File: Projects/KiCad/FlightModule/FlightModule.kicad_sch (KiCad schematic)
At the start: 53 parts, among them J1 Conn_01x05_Socket, J2 Conn_01x04_Pin, J3 Conn_01x05_Pin, J4 Conn_01x02_Pin, J5 Conn_01x02_Pin, J6 Conn_01x02_Pin, J7 Conn_01x02_Pin, J8 Conn_01x02_Pin, SW1 SW_Push, SW2 SW_Push, U1 NUCLEO-F303K8, U2 MCP2562-E-P, U3 TLP222A, U4 TLP222A, U5 MB85RS2MT

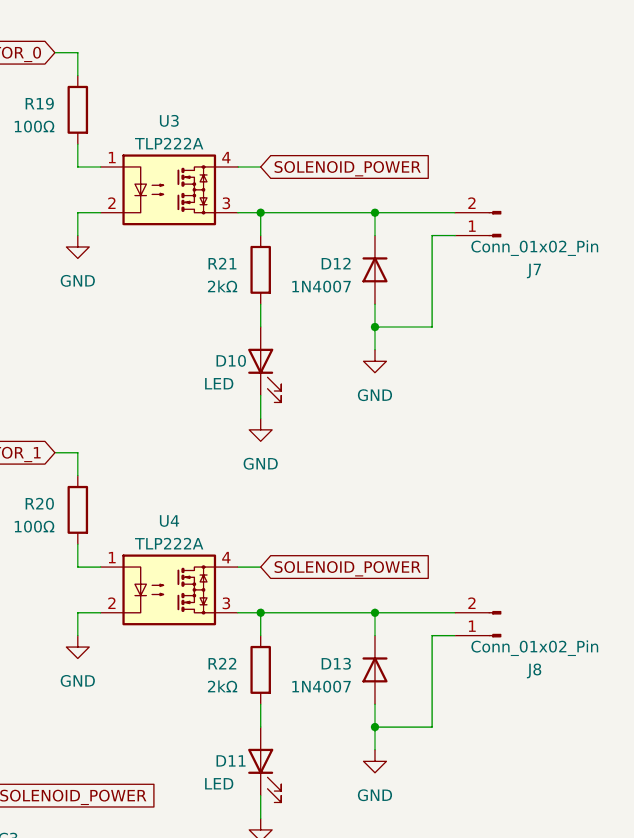
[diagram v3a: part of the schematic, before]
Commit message: ソレノイドのサージキラー回路に整流用ダイオードを追加
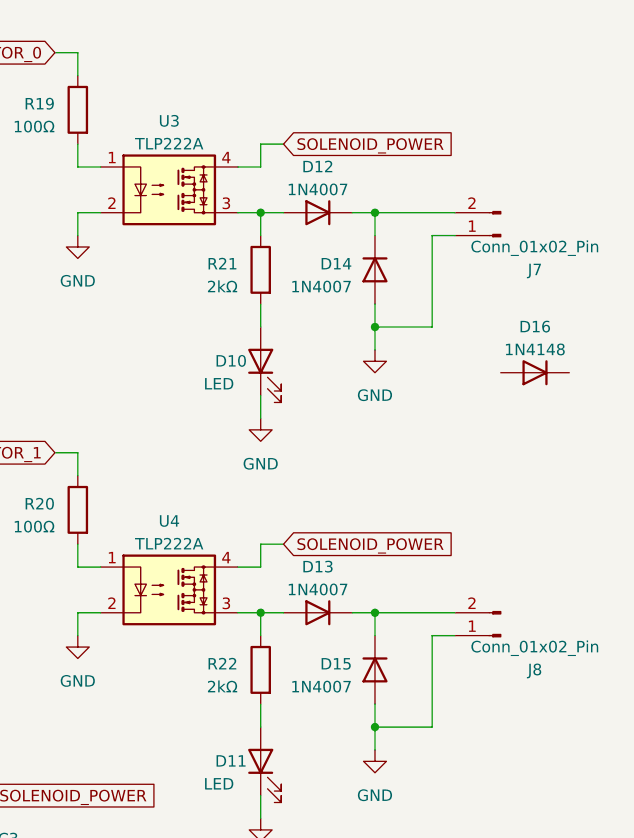
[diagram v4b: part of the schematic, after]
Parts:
- added D12, D13: 1N4007, Diode_THT:D_DO-41_SOD81_P10.16mm_Horizontal, symbol Diode:1N4007
- added D16: 1N4148, Diode_THT:D_DO-35_SOD27_P7.62mm_Horizontal, symbol Diode:1N4148
- renumbered D12 to D14, D13 to D15
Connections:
- net at R22.1, U4.3: now also D13.2 (A); no longer D15.1 (K), J8.2 (Pin_2)
- net at D14.1 (K), J7.2 (Pin_2): now also D12.1 (K); no longer R21.1, U3.3
- new net: D12.2 (A), R21.1, U3.3
- new net: D13.1 (K), D15.1 (K), J8.2 (Pin_2)
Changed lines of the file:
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@@
 (kicad_sch (version 20230121) (generator eeschema)
   (paper "A4")
+  (junction (at 246.38 38.1) (diameter 0) (color 0 0 0 0)
+  )
   (junction (at 115.57 110.49) (diameter 0) (color 0 0 0 0)
   )
@@
   (junction (at 163.83 114.3) (diameter 0) (color 0 0 0 0)
   )
+  (junction (at 222.25 143.51) (diameter 0) (color 0 0 0 0)
+  )
+  (junction (at 190.5 114.3) (diameter 0) (color 0 0 0 0)
+  )
+  (junction (at 213.36 102.87) (diameter 0) (color 0 0 0 0)
+  )
+  (junction (at 259.08 38.1) (diameter 0) (color 0 0 0 0)
+  )
+  (junction (at 229.87 140.97) (diameter 0) (color 0 0 0 0)
+  )
   (junction (at 246.38 82.55) (diameter 0) (color 0 0 0 0)
   )
-  (junction (at 222.25 143.51) (diameter 0) (color 0 0 0 0)
-  )
   (junction (at 259.08 82.55) (diameter 0) (color 0 0 0 0)
-  )
-  (junction (at 190.5 114.3) (diameter 0) (color 0 0 0 0)
-  )
-  (junction (at 246.38 38.1) (diameter 0) (color 0 0 0 0)
-  )
-  (junction (at 213.36 102.87) (diameter 0) (color 0 0 0 0)
-  )
-  (junction (at 259.08 38.1) (diameter 0) (color 0 0 0 0)
-  )
-  (junction (at 229.87 140.97) (diameter 0) (color 0 0 0 0)
   )
   (junction (at 242.57 151.13) (diameter 0) (color 0 0 0 0)
@@
     (stroke (width 0) (type default))
   )
-  (wire (pts (xy 243.84 77.47) (xy 246.38 77.47))
+  (wire (pts (xy 246.38 74.93) (xy 248.92 74.93))
     (stroke (width 0) (type default))
   )
@@
     (stroke (width 0) (type default))
   )
+  (wire (pts (xy 246.38 74.93) (xy 246.38 77.47))
+    (stroke (width 0) (type default))
+  )
   (wire (pts (xy 43.18 31.75) (xy 48.26 31.75))
     (stroke (width 0) (type default))
@@
     (stroke (width 0) (type default))
   )
+  (wire (pts (xy 246.38 30.48) (xy 246.38 33.02))
+    (stroke (width 0) (type default))
+  )
   (wire (pts (xy 27.94 34.29) (xy 40.64 34.29))
     (stroke (width 0) (type default))
@@
     (stroke (width 0) (type default))
   )
-  (wire (pts (xy 246.38 82.55) (xy 259.08 82.55))
-    (stroke (width 0) (type default))
-  )
   (wire (pts (xy 43.18 34.29) (xy 48.26 34.29))
     (stroke (width 0) (type default))
@@
     (stroke (width 0) (type default))
   )
-  (wire (pts (xy 246.38 38.1) (xy 259.08 38.1))
-    (stroke (width 0) (type default))
-  )
   (bus (pts (xy 43.18 53.34) (xy 43.18 55.88))
     (stroke (width 0) (type default))
@@
     (stroke (width 0) (type default))
   )
+  (wire (pts (xy 256.54 38.1) (xy 259.08 38.1))
+    (stroke (width 0) (type default))
+  )
   (wire (pts (xy 259.08 38.1) (xy 259.08 40.64))
     (stroke (width 0) (type default))
@@
     (stroke (width 0) (type default))
   )
+  (wire (pts (xy 246.38 82.55) (xy 248.92 82.55))
+    (stroke (width 0) (type default))
+  )
   (wire (pts (xy 190.5 124.46) (xy 190.5 127))
     (stroke (width 0) (type default))
@@
     (stroke (width 0) (type default))
   )
+  (wire (pts (xy 246.38 38.1) (xy 248.92 38.1))
+    (stroke (width 0) (type default))
+  )
   (wire (pts (xy 139.7 43.18) (xy 139.7 45.72))
     (stroke (width 0) (type default))
@@
     (stroke (width 0) (type default))
   )
+  (wire (pts (xy 246.38 77.47) (xy 243.84 77.47))
+    (stroke (width 0) (type default))
+  )
   (wire (pts (xy 259.08 82.55) (xy 259.08 85.09))
     (stroke (width 0) (type default))
@@
     (stroke (width 0) (type default))
   )
+  (wire (pts (xy 246.38 33.02) (xy 243.84 33.02))
+    (stroke (width 0) (type default))
+  )
   (wire (pts (xy 242.57 130.81) (xy 242.57 133.35))
     (stroke (width 0) (type default))
@@
     (stroke (width 0) (type default))
   )
+  (wire (pts (xy 256.54 82.55) (xy 259.08 82.55))
+    (stroke (width 0) (type default))
+  )
   (wire (pts (xy 134.62 110.49) (xy 137.16 110.49))
     (stroke (width 0) (type default))
@@
     (stroke (width 0) (type default))
   )
-  (wire (pts (xy 243.84 33.02) (xy 246.38 33.02))
+  (wire (pts (xy 246.38 30.48) (xy 248.92 30.48))
     (stroke (width 0) (type default))
   )
@@
     )
   )
-  (global_label "SOLENOID_POWER" (shape input) (at 246.38 33.02 0) (fields_autoplaced)
-    (effects (font (size 1.27 1.27)) (justify left))
-    (property "Intersheetrefs" "${INTERSHEET_REFS}" (at 265.9772 33.02 0)
+  (global_label "SOLENOID_POWER" (shape input) (at 248.92 30.48 0) (fields_autoplaced)
+    (effects (font (size 1.27 1.27)) (justify left))
+    (property "Intersheetrefs" "${INTERSHEET_REFS}" (at 268.5172 30.48 0)
       (effects (font (size 1.27 1.27)) (justify left) hide)
     )
@@
     )
   )
-  (global_label "SOLENOID_POWER" (shape input) (at 246.38 77.47 0) (fields_autoplaced)
-    (effects (font (size 1.27 1.27)) (justify left))
-    (property "Intersheetrefs" "${INTERSHEET_REFS}" (at 265.9772 77.47 0)
+  (global_label "SOLENOID_POWER" (shape input) (at 248.92 74.93 0) (fields_autoplaced)
+    (effects (font (size 1.27 1.27)) (justify left))
+    (property "Intersheetrefs" "${INTERSHEET_REFS}" (at 268.5172 74.93 0)
       (effects (font (size 1.27 1.27)) (justify left) hide)
     )
@@
   (symbol (lib_id "Diode:1N4007") (at 259.08 44.45 90) (mirror x) (unit 1)
     (in_bom yes) (on_board yes) (dnp no) (fields_autoplaced)
-    (property "Reference" "D12" (at 256.54 43.815 90)
+    (property "Reference" "D14" (at 256.54 43.815 90)
       (effects (font (size 1.27 1.27)) (justify left))
     )
@@
       (project "FlightModule"
         (path "/ea1ed597-7cd3-4340-902e-bdce8f2d7a62"
-          (reference "D12") (unit 1)
+          (reference "D14") (unit 1)
         )
       )
@@
         (path "/ea1ed597-7cd3-4340-902e-bdce8f2d7a62"
           (reference "#PWR017") (unit 1)
+        )
+      )
+    )
+  )
+  (symbol (lib_id "Diode:1N4148") (at 276.86 55.88 180) (unit 1)
+    (in_bom yes) (on_board yes) (dnp no) (fields_autoplaced)
+    (property "Reference" "D16" (at 276.86 50.8 0)
+      (effects (font (size 1.27 1.27)))
+    )
+    (property "Value" "1N4148" (at 276.86 53.34 0)
+      (effects (font (size 1.27 1.27)))
+    )
+    (property "Footprint" "Diode_THT:D_DO-35_SOD27_P7.62mm_Horizontal" (at 276.86 55.88 0)
+      (effects (font (size 1.27 1.27)) hide)
+    )
+    (property "Datasheet" "https://assets.nexperia.com/documents/data-sheet/1N4148_1N4448.pdf" (at 276.86 55.88 0)
+      (effects (font (size 1.27 1.27)) hide)
+    )
+    (property "Sim.Device" "D" (at 276.86 55.88 0)
+      (effects (font (size 1.27 1.27)) hide)
+    )
+    (property "Sim.Pins" "1=K 2=A" (at 276.86 55.88 0)
+      (effects (font (size 1.27 1.27)) hide)
+    )
+    (pin "1")
+    (pin "2")
+    (instances
+      (project "FlightModule"
+        (path "/ea1ed597-7cd3-4340-902e-bdce8f2d7a62"
+          (reference "D16") (unit 1)
         )
       )
@@
         (path "/ea1ed597-7cd3-4340-902e-bdce8f2d7a62"
           (reference "R12") (unit 1)
+        )
+      )
+    )
+  )
+  (symbol (lib_id "Diode:1N4007") (at 252.73 82.55 0) (mirror y) (unit 1)
+    (in_bom yes) (on_board yes) (dnp no) (fields_autoplaced)
+    (property "Reference" "D13" (at 252.73 77.47 0)
+      (effects (font (size 1.27 1.27)))
+    )
+    (property "Value" "1N4007" (at 252.73 80.01 0)
+      (effects (font (size 1.27 1.27)))
+    )
+    (property "Footprint" "Diode_THT:D_DO-41_SOD81_P10.16mm_Horizontal" (at 252.73 86.995 0)
+      (effects (font (size 1.27 1.27)) hide)
+    )
+    (property "Datasheet" "http://www.vishay.com/docs/88503/1n4001.pdf" (at 252.73 82.55 0)
+      (effects (font (size 1.27 1.27)) hide)
+    )
+    (property "Sim.Device" "D" (at 252.73 82.55 0)
+      (effects (font (size 1.27 1.27)) hide)
+    )
+    (property "Sim.Pins" "1=K 2=A" (at 252.73 82.55 0)
+      (effects (font (size 1.27 1.27)) hide)
+    )
+    (pin "1")
+    (pin "2")
+    (instances
+      (project "FlightModule"
+        (path "/ea1ed597-7cd3-4340-902e-bdce8f2d7a62"
+          (reference "D13") (unit 1)
         )
       )
@@
     )
   )
+  (symbol (lib_id "Diode:1N4007") (at 252.73 38.1 0) (mirror y) (unit 1)
+    (in_bom yes) (on_board yes) (dnp no) (fields_autoplaced)
+    (property "Reference" "D12" (at 252.73 33.02 0)
+      (effects (font (size 1.27 1.27)))
+    )
+    (property "Value" "1N4007" (at 252.73 35.56 0)
+      (effects (font (size 1.27 1.27)))
+    )
+    (property "Footprint" "Diode_THT:D_DO-41_SOD81_P10.16mm_Horizontal" (at 252.73 42.545 0)
+      (effects (font (size 1.27 1.27)) hide)
+    )
+    (property "Datasheet" "http://www.vishay.com/docs/88503/1n4001.pdf" (at 252.73 38.1 0)
+      (effects (font (size 1.27 1.27)) hide)
+    )
+    (property "Sim.Device" "D" (at 252.73 38.1 0)
+      (effects (font (size 1.27 1.27)) hide)
+    )
+    (property "Sim.Pins" "1=K 2=A" (at 252.73 38.1 0)
+      (effects (font (size 1.27 1.27)) hide)
+    )
+    (pin "1")
+    (pin "2")
+    (instances
+      (project "FlightModule"
+        (path "/ea1ed597-7cd3-4340-902e-bdce8f2d7a62"
+          (reference "D12") (unit 1)
+        )
+      )
+    )
+  )
   (symbol (lib_id "power:+12V") (at 35.56 73.66 0) (unit 1)
     (in_bom yes) (on_board yes) (dnp no) (fields_autoplaced)
@@
   (symbol (lib_id "Diode:1N4007") (at 259.08 88.9 90) (mirror x) (unit 1)
     (in_bom yes) (on_board yes) (dnp no) (fields_autoplaced)
-    (property "Reference" "D13" (at 256.54 88.265 90)
+    (property "Reference" "D15" (at 256.54 88.265 90)
       (effects (font (size 1.27 1.27)) (justify left))
     )
@@
       (project "FlightModule"
         (path "/ea1ed597-7cd3-4340-902e-bdce8f2d7a62"
-          (reference "D13") (unit 1)
-        )
-      )
+          (reference "D15") (unit 1)
+        )
+      )

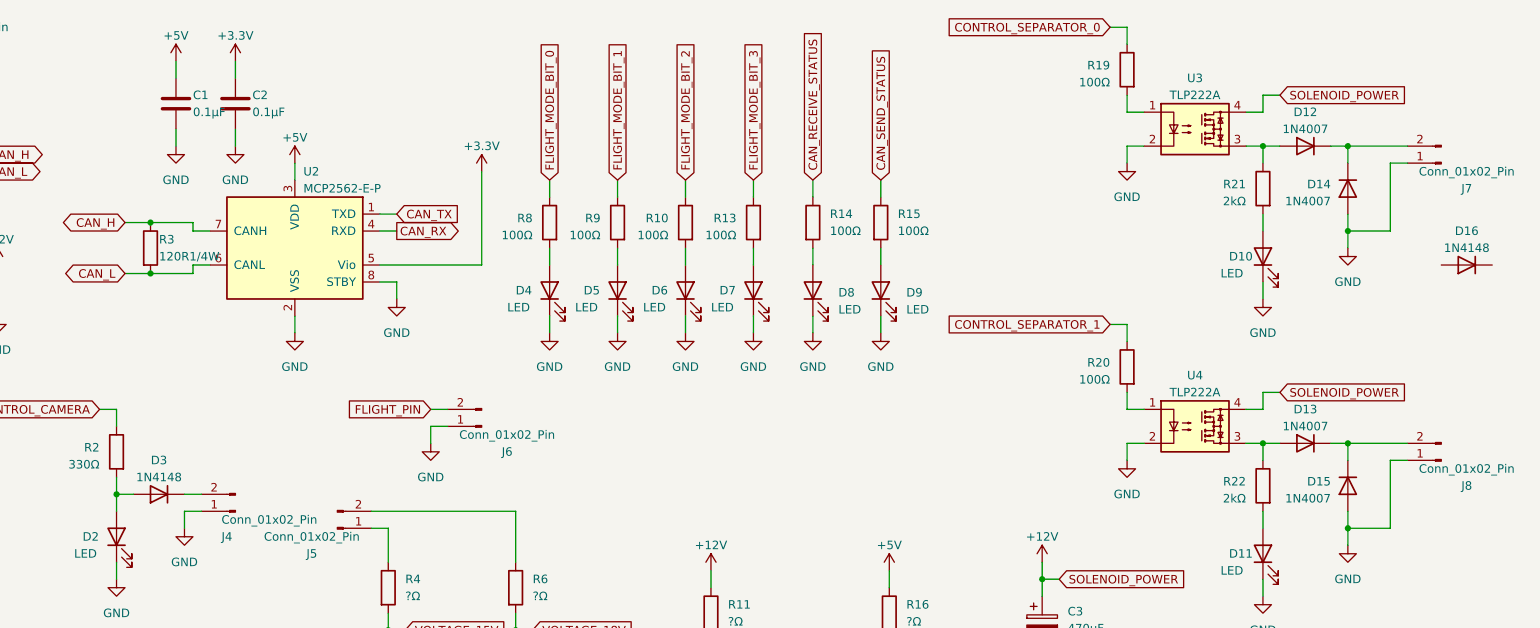
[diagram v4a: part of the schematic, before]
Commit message: ダイオードをSMDに変更
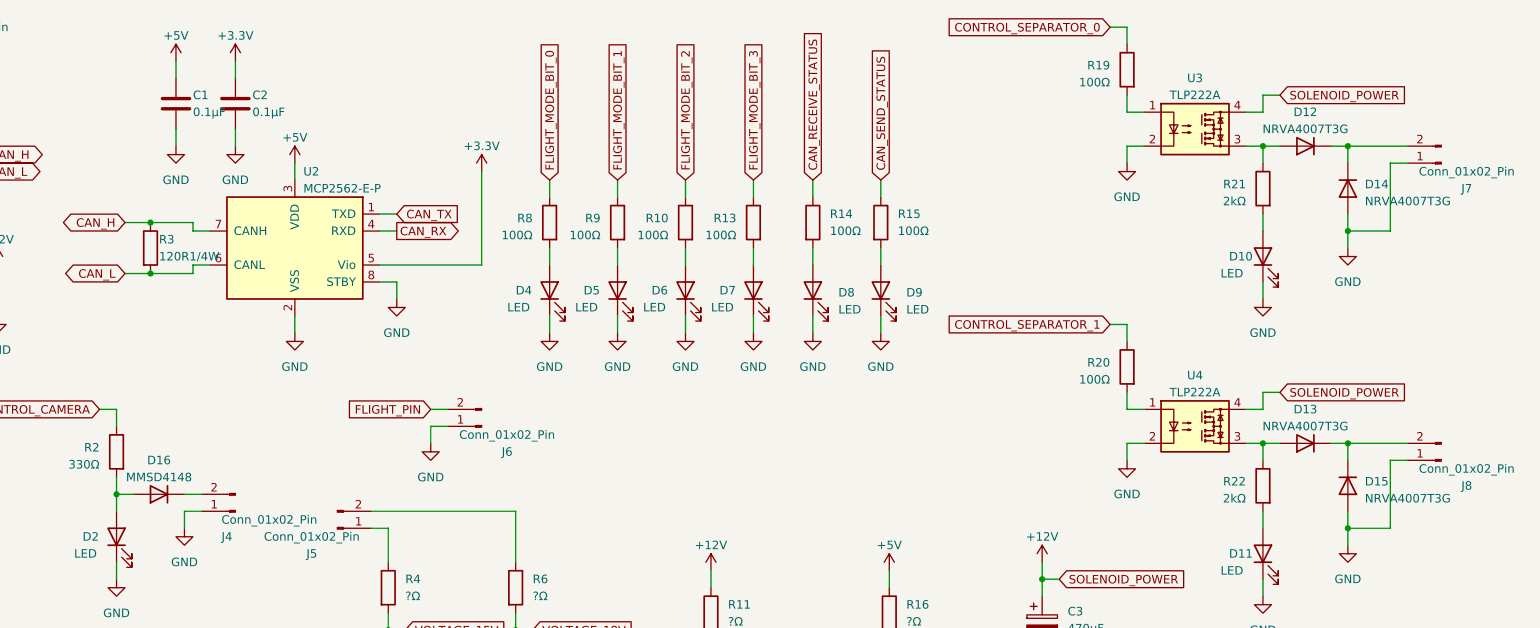
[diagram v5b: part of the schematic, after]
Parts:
- removed D12, D13, D14, D15: 1N4007, Diode_THT:D_DO-41_SOD81_P10.16mm_Horizontal, symbol Diode:1N4007
- removed D16, D3: 1N4148, Diode_THT:D_DO-35_SOD27_P7.62mm_Horizontal, symbol Diode:1N4148
- added D12, D13, D14, D15: NRVA4007T3G, Diode_SMD:D_SMA, symbol Diode:NRVA4007T3G
- added D16: MMSD4148, Diode_SMD:D_SOD-123, symbol Diode:MMSD4148
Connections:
- net GND: now also D14.2 (A), D15.2 (A)
- net at R22.1, U4.3: now also D13.2 (A)
- net at J7.2 (Pin_2): now also D12.1 (K), D14.1 (K)
- net at J4.2 (Pin_2): now also D16.1 (K)
- net at D2.2 (A), R2.2: now also D16.2 (A)
- net at R21.1, U3.3: now also D12.2 (A)
- net at J8.2 (Pin_2): now also D13.1 (K), D15.1 (K)

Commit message: 一通り部品を選定
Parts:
- removed D12, D13, D14, D15: NRVA4007T3G, Diode_SMD:D_SMA, symbol Diode:NRVA4007T3G
- removed D16: MMSD4148, Diode_SMD:D_SOD-123, symbol Diode:MMSD4148
- added D11, D12, D13, D14: 1N4007, Diode_SMD:D_SOD-123F, symbol Diode:1N4007
- added R23, R24: 120Ω, Resistor_SMD:R_0603_1608Metric_Pad0.98x0.95mm_HandSolder, symbol Device:R
- C3: value 470μF -> 100μF; footprint Capacitor_THT:CP_Radial_D10.0mm_P3.50mm -> Capacitor_SMD:CP_Elec_6.3x7.7
- D1, D2: value LED -> RED; footprint LED_SMD:LED_1206_3216Metric_Pad1.42x1.75mm_HandSolder -> LED_SMD:LED_0603_1608Metric_Pad1.05x0.95mm_HandSolder
- D10: renamed from D11; value LED -> GREEN; footprint LED_SMD:LED_1206_3216Metric_Pad1.42x1.75mm_HandSolder -> LED_SMD:LED_0603_1608Metric_Pad1.05x0.95mm_HandSolder
- D3: renamed from D4; value LED -> GREEN; footprint LED_SMD:LED_1206_3216Metric_Pad1.42x1.75mm_HandSolder -> LED_SMD:LED_0603_1608Metric_Pad1.05x0.95mm_HandSolder
- D4: renamed from D5; value LED -> GREEN; footprint LED_SMD:LED_1206_3216Metric_Pad1.42x1.75mm_HandSolder -> LED_SMD:LED_0603_1608Metric_Pad1.05x0.95mm_HandSolder
- D5: renamed from D6; value LED -> GREEN; footprint LED_SMD:LED_1206_3216Metric_Pad1.42x1.75mm_HandSolder -> LED_SMD:LED_0603_1608Metric_Pad1.05x0.95mm_HandSolder
- D6: renamed from D7; value LED -> GREEN; footprint LED_SMD:LED_1206_3216Metric_Pad1.42x1.75mm_HandSolder -> LED_SMD:LED_0603_1608Metric_Pad1.05x0.95mm_HandSolder
- D7: renamed from D8; value LED -> ORANGE; footprint LED_SMD:LED_1206_3216Metric_Pad1.42x1.75mm_HandSolder -> LED_SMD:LED_0603_1608Metric_Pad1.05x0.95mm_HandSolder
- D8: renamed from D9; value LED -> ORANGE; footprint LED_SMD:LED_1206_3216Metric_Pad1.42x1.75mm_HandSolder -> LED_SMD:LED_0603_1608Metric_Pad1.05x0.95mm_HandSolder
- D9: renamed from D10; value LED -> GREEN; footprint LED_SMD:LED_1206_3216Metric_Pad1.42x1.75mm_HandSolder -> LED_SMD:LED_0603_1608Metric_Pad1.05x0.95mm_HandSolder
- R1, R14, R15, R18, R21, R22, R3: footprint Resistor_SMD:R_0805_2012Metric_Pad1.20x1.40mm_HandSolder -> Resistor_SMD:R_0603_1608Metric_Pad0.98x0.95mm_HandSolder
- R10, R13, R8, R9: value 100Ω -> 300Ω; footprint Resistor_SMD:R_0805_2012Metric_Pad1.20x1.40mm_HandSolder -> Resistor_SMD:R_0603_1608Metric_Pad0.98x0.95mm_HandSolder
- R11: value ?Ω -> 3kΩ; footprint Resistor_SMD:R_0805_2012Metric_Pad1.20x1.40mm_HandSolder -> Resistor_SMD:R_0603_1608Metric_Pad0.98x0.95mm_HandSolder
- R12: value ?Ω -> 750Ω; footprint Resistor_SMD:R_0805_2012Metric_Pad1.20x1.40mm_HandSolder -> Resistor_SMD:R_0603_1608Metric_Pad0.98x0.95mm_HandSolder
- R16: value ?Ω -> 1.3kΩ; footprint Resistor_SMD:R_0805_2012Metric_Pad1.20x1.40mm_HandSolder -> Resistor_SMD:R_0603_1608Metric_Pad0.98x0.95mm_HandSolder
- R17: value ?Ω -> 1.2kΩ; footprint Resistor_SMD:R_0805_2012Metric_Pad1.20x1.40mm_HandSolder -> Resistor_SMD:R_0603_1608Metric_Pad0.98x0.95mm_HandSolder
- R19, R20: value 100Ω -> 120Ω; footprint Resistor_SMD:R_0805_2012Metric_Pad1.20x1.40mm_HandSolder -> Resistor_SMD:R_0603_1608Metric_Pad0.98x0.95mm_HandSolder
- R2: value 330Ω -> 300Ω; footprint Resistor_SMD:R_0805_2012Metric_Pad1.20x1.40mm_HandSolder -> Resistor_SMD:R_0603_1608Metric_Pad0.98x0.95mm_HandSolder
- R4: value ?Ω -> 4.3kΩ; footprint Resistor_SMD:R_0805_2012Metric_Pad1.20x1.40mm_HandSolder -> Resistor_SMD:R_0603_1608Metric_Pad0.98x0.95mm_HandSolder
- R5, R7: value ?Ω -> 820Ω; footprint Resistor_SMD:R_0805_2012Metric_Pad1.20x1.40mm_HandSolder -> Resistor_SMD:R_0603_1608Metric_Pad0.98x0.95mm_HandSolder
- R6: value ?Ω -> 5.6kΩ; footprint Resistor_SMD:R_0805_2012Metric_Pad1.20x1.40mm_HandSolder -> Resistor_SMD:R_0603_1608Metric_Pad0.98x0.95mm_HandSolder
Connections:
- net GND: now also D13.2 (A), D14.2 (A), R23.2, R24.2
- net at R22.1, U4.3: now also D12.2 (A)
- net at J7.2 (Pin_2): now also D11.1 (K), D13.1 (K)
- net at R21.1, U3.3: now also D11.2 (A)
- net at J4.2 (Pin_2): now also D2.2 (A), R2.2
- net at J8.2 (Pin_2): now also D12.1 (K), D14.1 (K)
- net at R20.2, U4.1: now also R24.1
- net at R19.2, U3.1: now also R23.1
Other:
- moved on the sheet: C1, C2, D1, D2, D3, D4, D5, D6, D7, D8, J4, R1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
